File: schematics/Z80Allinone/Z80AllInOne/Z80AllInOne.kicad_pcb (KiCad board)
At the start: 2 copper layers, 389.9 x 174 mm, 174 parts, among them J1 USB_B_Micro, J10 CF Card IDE, J2 USER_IO_CONN, J3 COMP_VIDEOUT, J4 TTL SERIAL, J5 USR_INTR, J6 CASETTE/AUDIO, J7 KEYBOARD_HEADER, J8 TRGS/TOS, K1 FINDER-30.22, Q1 IRLML6402, Q2 2N3904, Q3 BC337, Q4 BC337, SW1 SW_DIP_x04, SW2 RESET, U1 Z80CPU, U10 74LS574, U11 AS6C62256-55PCN, U12 7400, U13 7400, U14 74LS138, U15 74LS139, U16 74LS32, U17 74HC04, U2 MAIN RAM, U20 74LS02, U21 AY-3-8910, U22 LM386, U23 NA555P, U24 Z80-CTC, U25 74LS32, U26 74LS148, U27 74HC00, U28 74LS373, U29 L7805, U3 28C256, U4 82C55A, U5 16550, U6 FT232RL, U7 TMS9918A, U8 74LS574, U9 74LS574, X1 4MHz, Y2 10.73MHz

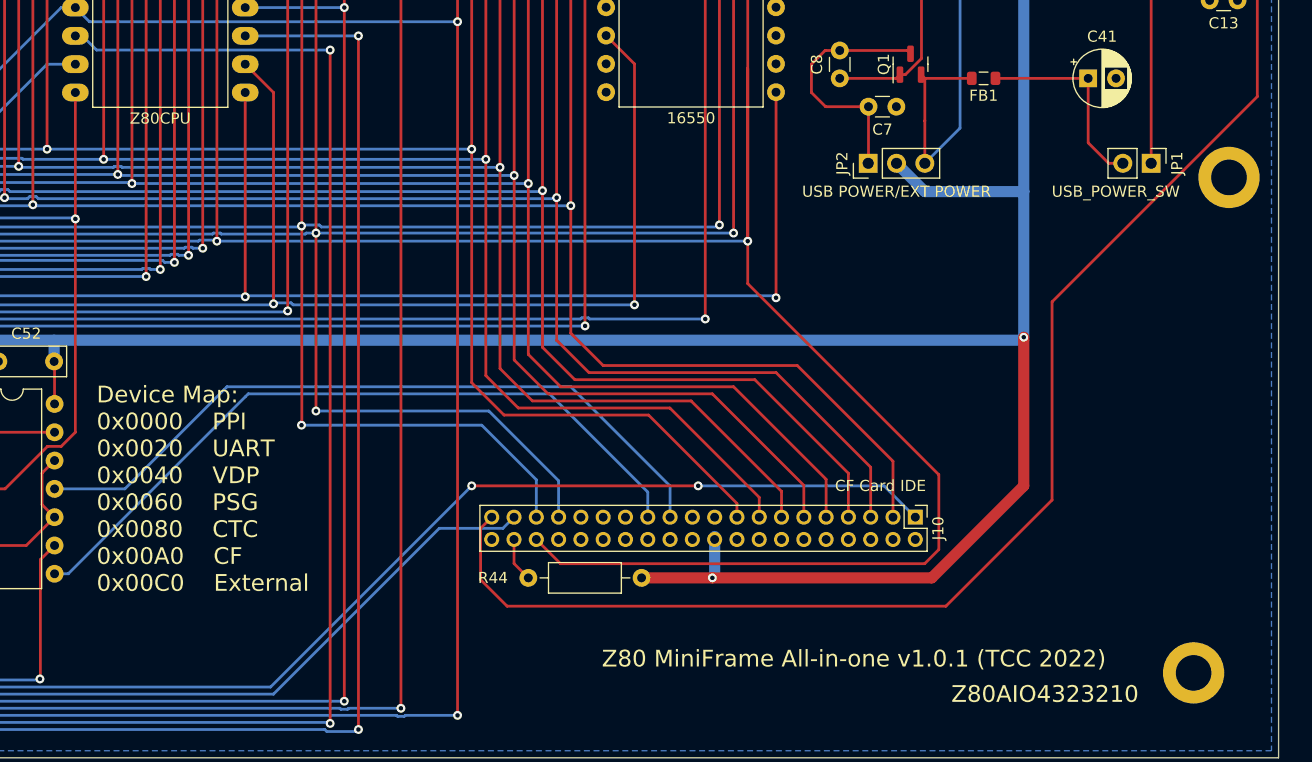
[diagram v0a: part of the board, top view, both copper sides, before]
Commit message: Latest code and schematic updates. Changed IDE connector to 2.54mm IDE connector
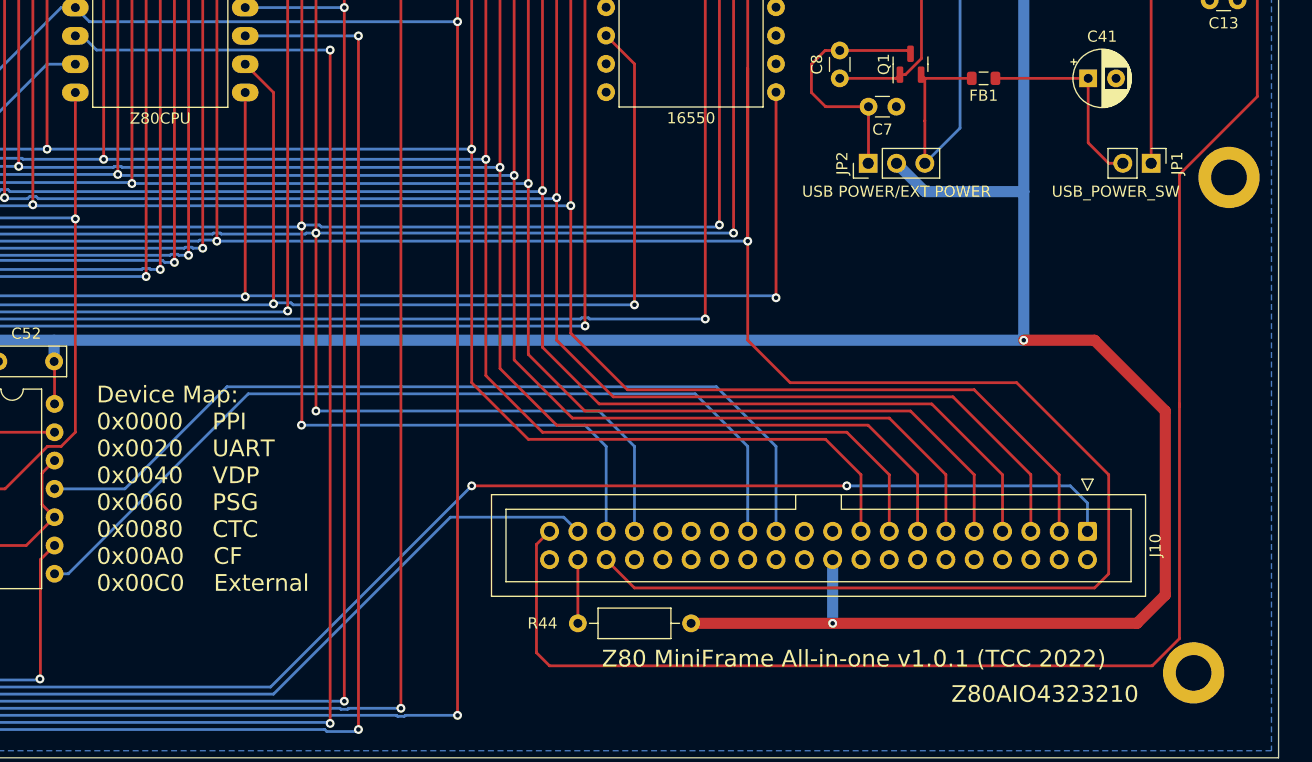
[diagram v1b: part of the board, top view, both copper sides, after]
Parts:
- J10: footprint Connector_PinHeader_2.00mm:PinHeader_2x20_P2.00mm_Vertical -> Connector_IDC:IDC-Header_2x20_P2.54mm_Vertical
- moved J10 15.5 mm to (386.7, 185.4)
- moved R44 6.03 mm to (341.0, 193.7)
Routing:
- net /IO/A2: track 641.5 -> 671.1 mm
- net VCC: track 1919.4 -> 1946.3 mm
- net /MR: track 137.2 -> 154.7 mm
- net Net-(J10-Pad39): track 160.6 -> 176.9 mm
- net /BUS Expansion/D7: track 762.3 -> 777.8 mm
- net /BUS Expansion/D6: track 771.2 -> 786.4 mm
- net /BUS Expansion/D5: track 776.3 -> 791.3 mm
- net /BUS Expansion/D4: track 780.4 -> 795.2 mm
- net /BUS Expansion/D3: track 786.8 -> 801.4 mm
- net /BUS Expansion/D2: track 763.5 -> 777.9 mm
- net /BUS Expansion/D1: track 744.2 -> 758.3 mm
- net /BUS Expansion/D0: track 731.9 -> 745.8 mm
- net /IOWR: track 65.5 -> 78.4 mm
- net /IORD: track 65.8 -> 78.5 mm
- net /IO/A1: track 692.3 -> 702.2 mm
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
